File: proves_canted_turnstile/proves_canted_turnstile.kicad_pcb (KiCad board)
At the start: 4 copper layers, 100 x 100 mm, 21 parts, among them J1 Conn_Coaxial, U1 QBA-07+, U2 QBA-07+, U3 QBA-07+

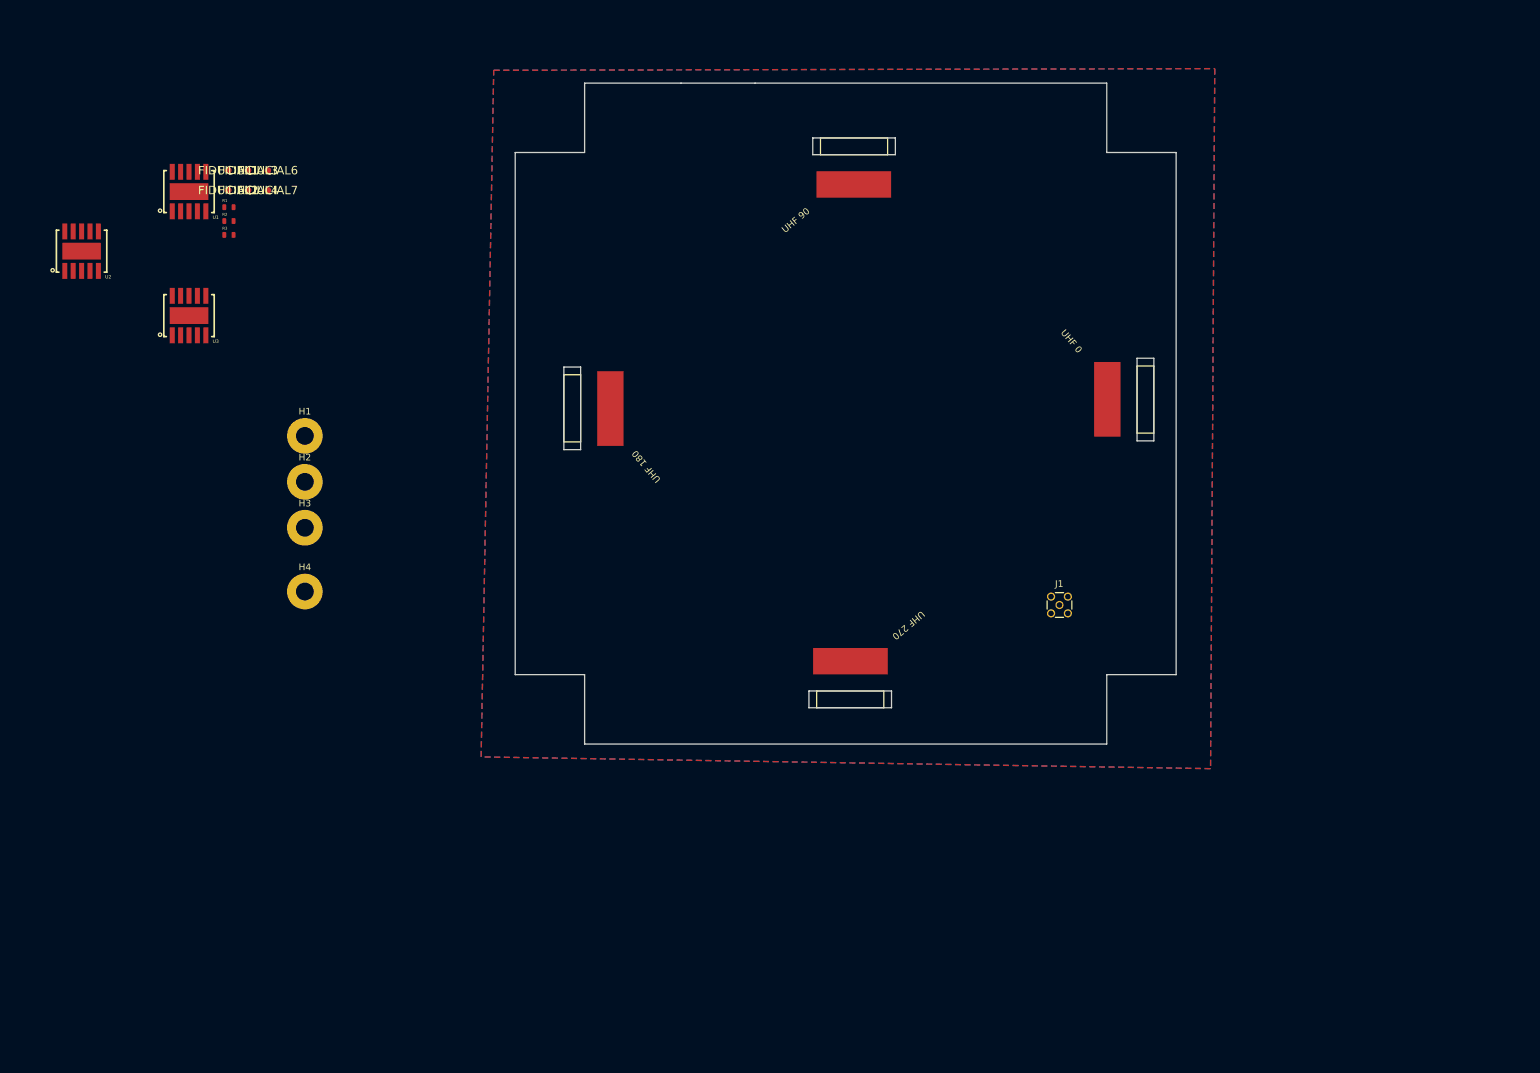
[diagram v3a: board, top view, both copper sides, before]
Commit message: changed trace widths
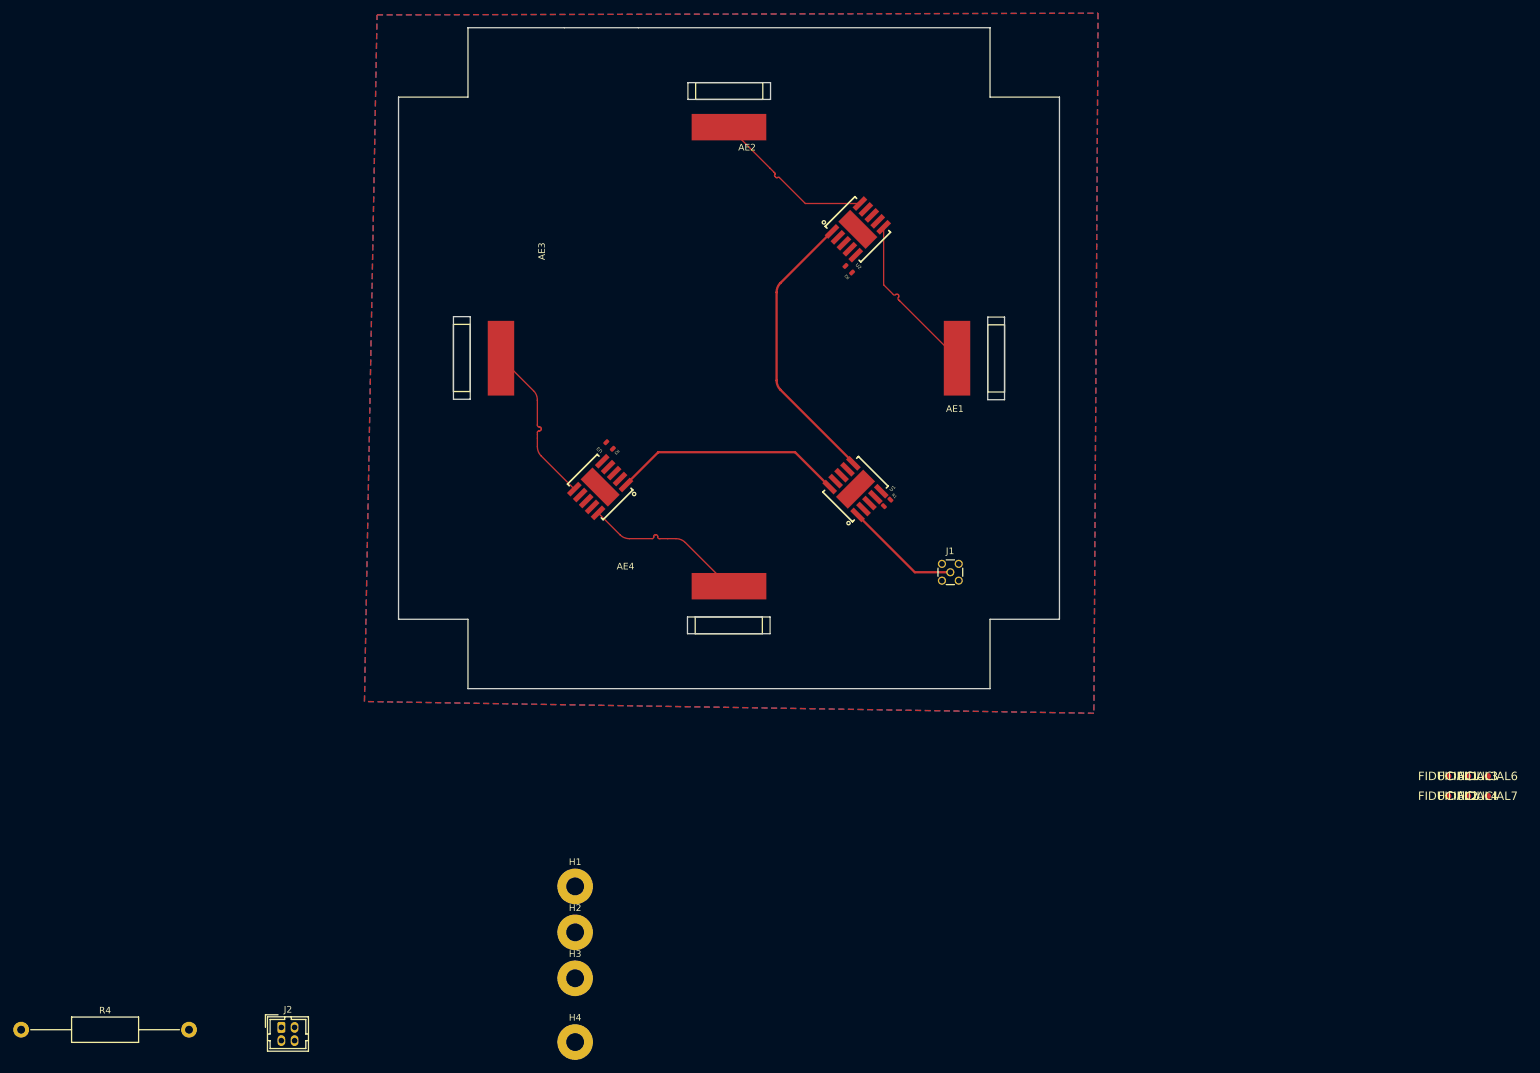
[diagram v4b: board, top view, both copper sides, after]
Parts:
- removed UHF 0: Antenna, Turnstile_Library:Singular_Tape_Measure_Antenna
- removed UHF 180: Antenna, Turnstile_Library:Singular_Tape_Measure_Antenna
- removed UHF 270: Antenna, Turnstile_Library:Singular_Tape_Measure_Antenna
- removed UHF 90: Antenna, Turnstile_Library:Singular_Tape_Measure_Antenna
- added AE1: Antenna, plusz-end-card-with-turnstile-mezzanine-eagle-import:Singular Tape Measure, F.Cu at (178.2, 82.5)
- added AE2: Antenna, plusz-end-card-with-turnstile-mezzanine-eagle-import:Singular Tape Measure, F.Cu at (143.7, 48.0)
- added AE3: Antenna, plusz-end-card-with-turnstile-mezzanine-eagle-import:Singular Tape Measure, F.Cu at (109.2, 82.5)
- added AE4: Antenna, plusz-end-card-with-turnstile-mezzanine-eagle-import:Singular Tape Measure, F.Cu at (143.7, 117.0)
- added J2: Conn_02x02_Counter_Clockwise, Connector_Hirose:Hirose_DF11-4DP-2DSA_2x02_P2.00mm_Vertical, F.Cu at (75.9, 183.8)
- added R4: R_Small_US, Resistor_THT:R_Axial_DIN0411_L9.9mm_D3.6mm_P25.40mm_Horizontal, F.Cu at (36.6, 184.2)
- moved FIDUCIAL1 206.1 mm to (252.5, 145.8)
- moved FIDUCIAL2 206.1 mm to (252.5, 148.8)
- moved FIDUCIAL3 206.1 mm to (255.5, 145.8)
- moved FIDUCIAL4 206.1 mm to (255.5, 148.8)
- moved FIDUCIAL6 206.1 mm to (258.5, 145.8)
- moved FIDUCIAL7 206.1 mm to (258.5, 148.8)
- moved U2 117.5 mm to (163.2, 63.1), turned to -45 degrees
- moved U1 110.4 mm to (162.8, 102.4), turned to 45 degrees
- moved R1 109.2 mm to (167.6, 104.4), turned to 45 degrees
- moved R2 94.1 mm to (161.8, 69.1), turned to 135 degrees
- moved H2 79.5 mm to (120.4, 169.4)
- moved H3 79.5 mm to (120.4, 176.4)
- moved H4 79.5 mm to (120.4, 186.0)
- moved H1 79.5 mm to (120.4, 162.5)
- moved U3 67.4 mm to (124.2, 102.0), turned to 135 degrees
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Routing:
- net /UHF-SHORT: track 0.00 -> 43.2 mm
- net /UHF-SHORT+1/4WAVE: track 0.00 -> 35.1 mm
- net /UHF_90: track 0.00 -> 25.0 mm
- net /UHF_0: track 0.00 -> 25.0 mm
- net /UHF_270: track 0.00 -> 24.9 mm
- net /UHF_180: track 0.00 -> 24.9 mm
- net /UHF: track 0.00 -> 17.6 mm

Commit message: updates
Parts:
- moved J2 126.8 mm to (134.7, 71.4)
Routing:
- net /UHF-SHORT: track 43.2 -> 39.7 mm
- net /UHF_270: track 24.9 -> 24.2 mm
- net /UHF_180: track 24.9 -> 24.2 mm
- net /UHF_0: track 25.0 -> 24.4 mm

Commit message: updates
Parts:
- moved R3 0.28 mm to (125.6, 96.0)
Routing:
- net GND: track 0.00 -> 3.27 mm, vias 0 -> 3
- net Net-(U2-TERM): track 0.00 -> 2.28 mm
- net Net-(U3-TERM): track 0.00 -> 2.27 mm
- net Net-(U1-TERM): track 0.11 -> 1.90 mm
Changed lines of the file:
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@@
 	(footprint "plusz-end-card-with-turnstile-mezzanine-eagle-import:.0603-C-NOSILK"
 		(layer "F.Cu")
-		(at 125.603 95.758 -45)
+		(at 125.603 96.0374 -45)
 		(descr "0603 (metric 1608) tight 'IPC-C' without silkscreen\nIn house package for minimum spacing based on IPC-7351B. This package is identical to 0603-C, but has its tPlace silkscreen layer removed.")
 		(property "Reference" "R3"
@@
 		)
 		(property "Value" "50"
-			(at 0.736381 0.664539 135)
+			(at -0.664539 -1.167433 315)
 			(unlocked yes)
 			(layer "F.Fab")
@@
 	)
 	(segment
+		(start 125.108025 95.542425)
+		(end 125.057225 95.542425)
+		(width 0.2)
+		(layer "F.Cu")
+		(net 7)
+	)
+	(segment
+		(start 167.140172 104.935572)
+		(end 167.8432 105.6386)
+		(width 0.2)
+		(layer "F.Cu")
+		(net 7)
+	)
+	(segment
+		(start 125.057225 95.542425)
+		(end 124.2822 94.7674)
+		(width 0.2)
+		(layer "F.Cu")
+		(net 7)
+	)
+	(segment
+		(start 167.105224 104.935572)
+		(end 167.140172 104.935572)
+		(width 0.2)
+		(layer "F.Cu")
+		(net 7)
+	)
+	(segment
+		(start 162.292975 69.582975)
+		(end 163.068 70.358)
+		(width 0.2)
+		(layer "F.Cu")
+		(net 7)
+	)
+	(via
+		(at 124.2822 94.7674)
+		(size 0.6)
+		(drill 0.3)
+		(layers "F.Cu" "B.Cu")
+		(net 7)
+	)
+	(via
+		(at 163.068 70.358)
+		(size 0.6)
+		(drill 0.3)
+		(layers "F.Cu" "B.Cu")
+		(net 7)
+	)
+	(via
+		(at 167.8432 105.6386)
+		(size 0.6)
+		(drill 0.3)
+		(layers "F.Cu" "B.Cu")
+		(net 7)
+	)
+	(segment
 		(start 177.165 114.935)
 		(end 171.794898 114.935)
@@
 	)
 	(segment
+		(start 166.826215 102.676663)
+		(end 168.095174 103.945622)
+		(width 0.2)
+		(layer "F.Cu")
+		(net 9)
+	)
+	(segment
 		(start 166.720765 102.676663)
 		(end 166.826215 102.676663)
@@
 		(layer "F.Cu")
 		(net 9)
+	)
+	(segment
+		(start 161.303025 68.593025)
+		(end 162.855337 67.040713)
+		(width 0.2)
+		(layer "F.Cu")
+		(net 10)
+	)
+	(segment
+		(start 162.855337 67.040713)
+		(end 162.855337 66.958765)
+		(width 0.2)
+		(layer "F.Cu")
+		(net 10)
+	)
+	(segment
+		(start 124.495015 98.135335)
+		(end 126.097975 96.532375)
+		(width 0.2)
+		(layer "F.Cu")
+		(net 11)
+	)
+	(segment
+		(start 124.494563 98.135335)
+		(end 124.495015 98.135335)
+		(width 0.2)
+		(layer "F.Cu")
+		(net 11)
 	)
 	(segment
@@
 	)
 	(segment
-		(start 114.095213 87.467013)
+		(start 120.273135 93.644935)
 		(end 109.1748 82.5466)
-		(width 0.34925)
-		(layer "F.Cu")
-		(net 16)
-	)
-	(segment
-		(start 114.681 94.643751)
-		(end 114.681 88.884087)
-		(width 0.34925)
+		(width 0.38)
 		(layer "F.Cu")
 		(net 16)
@@
 	(segment
 		(start 120.273135 102.356763)
-		(end 115.266786 97.350414)
-		(width 0.34925)
+		(end 120.273135 93.644935)
+		(width 0.38)
 		(layer "F.Cu")
 		(net 16)
-	)
-	(segment
-		(start 114.681 88.884087)
-		(end 114.681 88.881227)
-		(width 0.34925)
-		(layer "F.Cu")
-		(net 16)
-	)
-	(segment
-		(start 114.681 95.936201)
-		(end 114.681 94.643751)
-		(width 0.34925)
-		(layer "F.Cu")
-		(net 16)
-	)
-	(arc
-		(start 115.266786 97.350414)
-		(mid 114.833241 96.701568)
-		(end 114.681 95.936201)
-		(width 0.34925)
-		(layer "F.Cu")
-		(net 16)
-	)
-	(arc
-		(start 114.681 88.881227)
-		(mid 114.528759 88.11586)
-		(end 114.095213 87.467013)
-		(width 0.34925)
-		(layer "F.Cu")
-		(net 16)
-	)
-	(segment
-		(start 137.068987 110.440787)
-		(end 143.6748 117.0466)
-		(width 0.34925)
-		(layer "F.Cu")
-		(net 17)
-	)
-	(segment
-		(start 134.418727 109.855)
-		(end 135.654773 109.855)
-		(width 0.34925)
-		(layer "F.Cu")
-		(net 17)
 	)
 	(segment
 		(start 123.865237 105.948865)
-		(end 127.185586 109.269214)
-		(width 0.34925)
+		(end 132.577065 105.948865)
+		(width 0.38)
 		(layer "F.Cu")
 		(net 17)
 	)
 	(segment
-		(start 128.599799 109.855)
-		(end 132.04694 109.855)
-		(width 0.34925)
+		(start 132.577065 105.948865)
+		(end 143.6748 117.0466)
+		(width 0.38)
 		(layer "F.Cu")
 		(net 17)
-	)
-	(segment
-		(start 132.04694 109.855)
-		(end 134.418727 109.855)
-		(width 0.34925)
-		(layer "F.Cu")
-		(net 17)
-	)
-	(arc
-		(start 135.654773 109.855)
-		(mid 136.42014 110.007241)
-		(end 137.068987 110.440787)
-		(width 0.34925)
-		(layer "F.Cu")
-		(net 17)
-	)
-	(arc
-		(start 127.185586 109.269214)
-		(mid 127.834432 109.702759)
-		(end 128.599799 109.855)
-		(width 0.34925)
-		(layer "F.Cu")
-		(net 17)

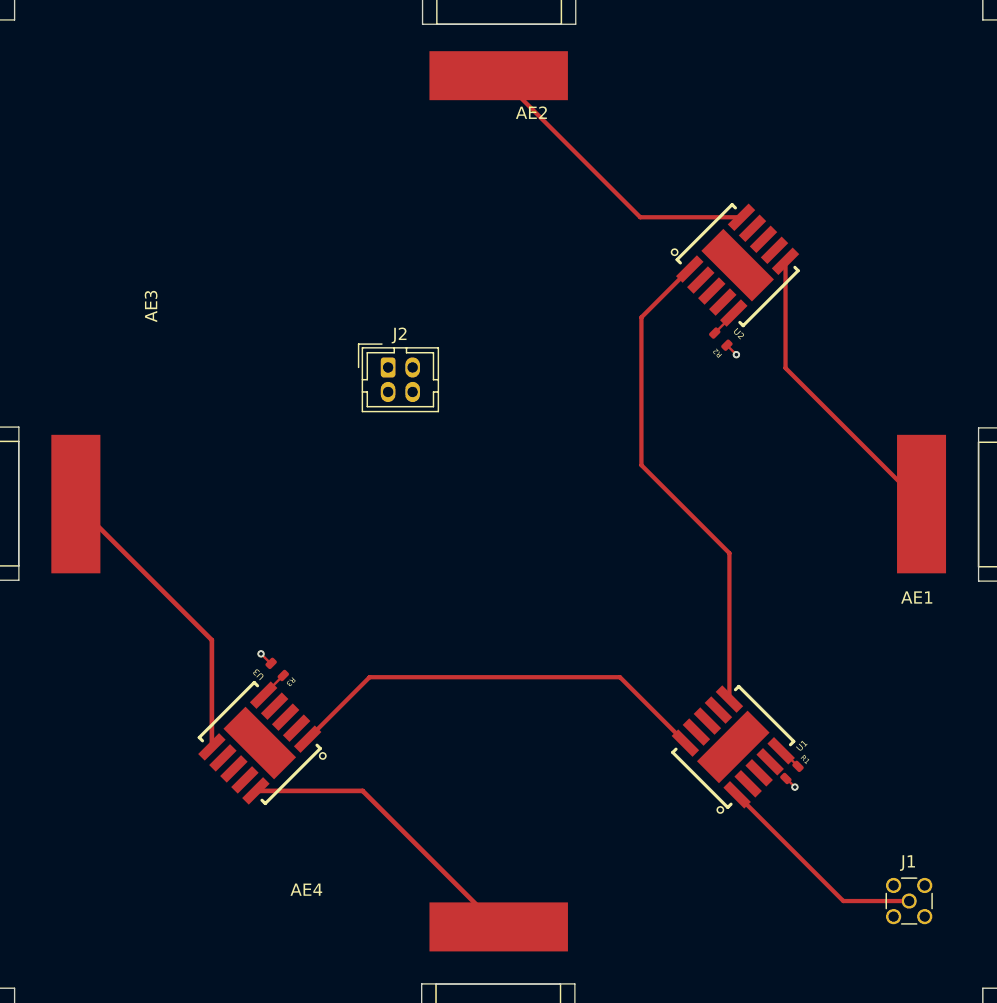
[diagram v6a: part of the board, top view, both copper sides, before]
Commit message: tuned lengths of U3 to 180 and 270 degree pads
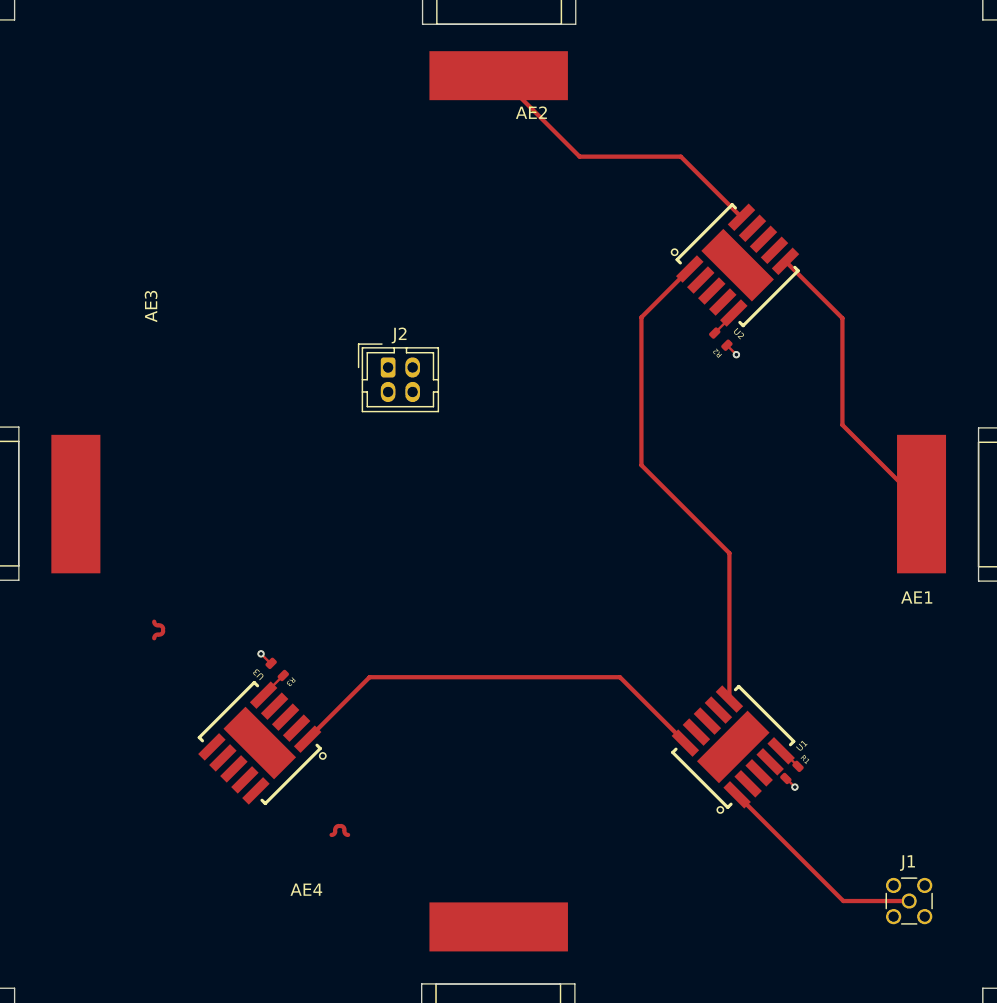
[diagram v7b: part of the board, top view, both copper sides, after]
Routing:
- net /UHF_270: track 24.4 -> 24.9 mm
- net /UHF_180: track 24.4 -> 24.9 mm

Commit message: finished critical traces
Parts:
- moved R4 38.6 mm to (66.5, 159.8)
- moved H1 3.00 mm to (122.7, 160.5)
- moved H2 3.00 mm to (122.7, 167.5)
- moved H3 3.00 mm to (122.7, 174.4)
- moved H4 3.00 mm to (122.7, 184.1)
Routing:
- net /UHF-SHORT+1/4WAVE: track 35.2 -> 135.7 mm
- net /UHF_0: track 24.4 -> 25.2 mm
- net /UHF-SHORT: track 39.7 -> 39.1 mm
- net /UHF_90: track 24.6 -> 25.2 mm
